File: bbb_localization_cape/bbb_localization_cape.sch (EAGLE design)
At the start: 31 parts, among them J1 CONN_04, J2 MOLEX-22-03-5035, U1 SN65HVD256DR, U2 ARDUCAMOV5642, U3 MSP430G2553IPW20R, U4 SN74LV1T126DCKR, U5 SN74LV1T125DCKR, U6 SN74LV1T126DCKR, U7 LP38693MP-3.3/NOPB, U8 LM1085ISX-ADJ

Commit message: Finished BOM
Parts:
- A1: ECE_STOCK (none) -> N; MANUFACTURER (none) -> Adafruit Industries LLC; MANUFACTURER_PART_NUMBER (none) -> 706; NOTES (none) -> 2 pack stacking header; PN (none) -> 1528-1365-ND; VENDOR (none) -> Digi-Key
- C1: ECE_STOCK (none) -> Y; LOCATION (none) -> R-3-074E, R-3-075; VENDOR (none) -> Digi-Key
- C2, C3: ECE_STOCK (none) -> N; MANUFACTURER (none) -> Murata Electronics North America; MANUFACTURER_PART_NUMBER (none) -> GRM21BR61C106KE15K; PN (none) -> 490-6473-1-ND; VENDOR (none) -> Digi-Key
- C4: ECE_STOCK (none) -> N; MANUFACTURER (none) -> Samsung Electro-Mechanics America, Inc.; MANUFACTURER_PART_NUMBER (none) -> CL21A226MOCLRNC; PN (none) -> 1276-6780-1-ND; VENDOR (none) -> Dig-Key
- C5: ECE_STOCK (none) -> Y; LOCATION (none) -> R-3-078C (D); VENDOR (none) -> Digi-Key
- C6: ECE_STOCK (none) -> N; MANUFACTURER (none) -> TDK Corporation; MANUFACTURER_PART_NUMBER (none) -> C3216X5R1A107M160AC; NOTES (none) -> Right at edge of rated voltage, consider larger form factor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; PN (none) -> 445-6007-1-ND; VENDOR (none) -> Digi-Key
- C7: ECE_STOCK (none) -> Y; LOCATION (none) -> R-3-078F; VENDOR (none) -> Digi-Key
- J1: ECE_STOCK (none) -> N; MANUFACTURER (none) -> JST Sales America Inc.; MANUFACTURER_PART_NUMBER (none) -> B4B-PH-K-S(LF)(SN); PN (none) -> 455-1706-ND; VENDOR (none) -> Digi-Key
- J2: ECE_STOCK (none) -> N; MANUFACTURER (none) -> Molex, LLC; MANUFACTURER_PART_NUMBER (none) -> 22-03-5035; PN (none) -> WM18887-ND; VENDOR (none) -> Digi-Key
- JP1: ECE_STOCK (none) -> N; MANUFACTURER (none) -> Samtec Inc.; MANUFACTURER_PART_NUMBER (none) -> SSW-104-01-F-S; PN (none) -> SAM10018-ND; VENDOR (none) -> Digi-Key
- PAD1, PAD2, SJ1, SJ2, SJ3: ECE_STOCK (none) -> N; VENDOR (none) -> OSH Park
- PS1: ECE_STOCK (none) -> N; MANUFACTURER (none) -> CUI Inc.; MANUFACTURER_PART_NUMBER (none) -> V7805-2000R; PN (none) -> 102-2188-ND; VENDOR (none) -> Digi-Key
- R1: ECE_STOCK (none) -> Y; LOCATION (none) -> R‐4‐033B; PN (none) -> P10.0KCCT‐ND; VENDOR (none) -> Digi-Key
- R2: ECE_STOCK (none) -> Y; LOCATION (none) -> R-4-033B; PN (none) -> P10.0KCCT-ND; VENDOR (none) -> Digi-Key
- R3: ECE_STOCK (none) -> Y; LOCATION (none) -> R‐4‐033B; MANUFACTURER_PART_NUMBER (none) -> ERJ-6ENF1002V; PN (none) -> P10.0KCCT-ND; VENDOR (none) -> Digi-Key
- R4: ECE_STOCK (none) -> N; MANUFACTURER (none) -> Stackpole Electronics Inc; MANUFACTURER_PART_NUMBER (none) -> RMCF0805JT47K0; NOTES (none) -> ECE stocks 0603; PN (none) -> RMCF0805JT47K0CT-ND; VENDOR (none) -> Digi-Key
- R5: ECE_STOCK (none) -> N; MANUFACTURER (none) -> Yageo; MANUFACTURER_PART_NUMBER (none) -> RC0805FR-07130RL; PN (none) -> 311-130CRCT-ND; VENDOR (none) -> Digi-Key
- R6: ECE_STOCK (none) -> N; MANUFACTURER (none) -> Yageo; MANUFACTURER_PART_NUMBER (none) -> RC0805FR-07910RL; PN (none) -> 311-910CRCT-ND; VENDOR (none) -> Digi-Key
- U1: ECE_STOCK (none) -> N; MANUFACTURER (none) -> Texas Instruments; PN (none) -> 296-30093-1-ND; VENDOR (none) -> DIGIKEY
- U2: ECE_STOCK (none) -> N; MANUFACTURER (none) -> Samtec Inc.; MANUFACTURER_PART_NUMBER (none) -> SSW-110-02-L-D; NOTES (none) -> 20 pin header; PN (none) -> SAM11952-ND; VENDOR (none) -> Digi-Key
- U3: ECE_STOCK (none) -> N; MANUFACTURER (none) -> Texas Instruments; NOTES (none) -> ECE stocks a different version; PN (none) -> 296-28430-1-ND; VENDOR (none) -> Digi-Key
- U4, U6: ECE_STOCK (none) -> N; MANUFACTURER (none) -> Texas Instruments; PN (none) -> 296-37175-1-ND; VENDOR (none) -> Digi-Key
- U5: ECE_STOCK (none) -> N; MANUFACTURER (none) -> Texas Instruments; PN (none) -> 296-37173-1-ND; VENDOR (none) -> Digi-Key
- U7: ECE_STOCK (none) -> N; MANUFACTURER (none) -> Texas Instruments; MANUFACTURER_PART_NUMBER (none) -> LP38693MP-3.3/NOPB; PN (none) -> LP38693MP-3.3/NOPBCT-ND; VENDOR (none) -> Digi-Key
- U8: ECE_STOCK (none) -> ?; MANUFACTURER (none) -> Texas Instruments; MANUFACTURER_PART_NUMBER (none) -> LM1085ISX-ADJ/NOPB; PN (none) -> LM1085ISX-ADJ/NOPBCT-ND; VENDOR (none) -> Digi-Key

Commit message: Updated pdf and other things
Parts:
- A1, C4, J2, JP1, PAD1, PAD2, PS1, R5, R6, SJ1, SJ2, SJ3, U2, U4, U5, U6: ECE_STOCK N -> (none)
- C1: ECE_STOCK Y -> (none); LOCATION R-3-074E, R-3-075 -> (none); MANUFACTURER (none) -> Samsung Electro-Mechanics America, Inc.; MANUFACTURER_PART_NUMBER (none) -> CL21B104KOANNNC; PN (none) -> 1276-2448-1-ND
- C2, C3: ECE_STOCK N -> (none); MANUFACTURER_PART_NUMBER GRM21BR61C106KE15K -> GRM21BR61E106MA73L; PN 490-6473-1-ND -> 490-10748-1-ND
- C5: ECE_STOCK Y -> (none); LOCATION R-3-078C (D) -> (none); MANUFACTURER (none) -> Samsung Electro-Mechanics America, Inc.; MANUFACTURER_PART_NUMBER (none) -> CL21B105KPFNNNE; PN (none) -> 1276-1275-1-ND
- C6: value 100uF -> 47uF; ECE_STOCK N -> (none); MANUFACTURER_PART_NUMBER C3216X5R1A107M160AC -> C3216X5R1E476M160AC; NOTES Right at edge of rated voltage, consider larger form factor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 -> Reduced capacitance from 100uF to 47uF, V2 package should b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; PN 445-6007-1-ND -> 445-8047-1-ND
- C7: ECE_STOCK Y -> (none); LOCATION R-3-078F -> (none); MANUFACTURER (none) -> Samsung Electro-Mechanics America, Inc.; MANUFACTURER_PART_NUMBER (none) -> CL21A475KQFNNNG; PN (none) -> 1276-6465-1-ND
- J1: ECE_STOCK N -> (none); MANUFACTURER_PART_NUMBER B4B-PH-K-S(LF)(SN) -> B4B-PH-K-S(LF)(SN)
- R1: ECE_STOCK Y -> (none); LOCATION R‐4‐033B -> (none); MANUFACTURER (none) -> Yageo; MANUFACTURER_PART_NUMBER (none) -> RC0805JR-0710KL; PN P10.0KCCT‐ND -> 311-10KARCT-ND
- R2: ECE_STOCK Y -> (none); LOCATION R-4-033B -> (none); MANUFACTURER (none) -> Yageo; MANUFACTURER_PART_NUMBER (none) -> RC0805JR-0710KL; PN P10.0KCCT-ND -> 311-10KARCT-ND
- R3: ECE_STOCK Y -> (none); LOCATION R‐4‐033B -> (none); MANUFACTURER (none) -> Yageo; MANUFACTURER_PART_NUMBER ERJ-6ENF1002V -> RC0805JR-0710KL; PN P10.0KCCT-ND -> 311-10KARCT-ND
- R4: ECE_STOCK N -> (none); MANUFACTURER_PART_NUMBER RMCF0805JT47K0 -> RMCF0805JT47K0; NOTES ECE stocks 0603 -> (none); PN RMCF0805JT47K0CT-ND -> RMCF0805JT47K0CT-ND
- U1: ECE_STOCK N -> (none); VENDOR DIGIKEY -> Digi-Key
- U3: ECE_STOCK N -> (none); PN 296-28430-1-ND -> 296-28430-1-ND
- U7: ECE_STOCK N -> (none); MANUFACTURER_PART_NUMBER LP38693MP-3.3/NOPB -> LP38693MP-3.3/NOPB; PN LP38693MP-3.3/NOPBCT-ND -> LP38693MP-3.3/NOPBCT-ND
- U8: ECE_STOCK ? -> (none)

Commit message: Changed board part from Adafruit to Sparkfun version
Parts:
- added B1: SPARKFUN_BEAGLE_BONE_BLACK_CAPE, SparkFun-Boards:SPARKFUN_BEAGLE_BONE_BLACK_CAPE
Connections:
- net +5V: now also B1P9.VDD_5V@1, B1P9.VDD_5V@2
- net DCAN1_RX: now also B1P9.GPIO_15
- net DCAN1_TX: now also B1P9.GPIO_14
- net GND: now also B1P8.DGND@1, B1P8.DGND@2, B1P9.DGND@1, B1P9.DGND@2, B1P9.DGND@3, B1P9.DGND@4, B1P9.DGND@5, B1P9.DGND@6
- net I2C2_SCL: now also B1P9.I2C2_SCL
- net I2C2_SDA: now also B1P9.I2C2_SDA
- net PRU1_0: now also B1P8.GPIO_70
- net PRU1_1: now also B1P8.GPIO_71
- net PRU1_10: now also B1P8.GPIO_88
- net PRU1_2: now also B1P8.GPIO_72
- net PRU1_3: now also B1P8.GPIO_73
- net PRU1_4: now also B1P8.GPIO_74
- net PRU1_5: now also B1P8.GPIO_75
- net PRU1_6: now also B1P8.GPIO_76
- net PRU1_7: now also B1P8.GPIO_77
- net PRU1_8: now also B1P8.GPIO_86
- net PRU1_9: now also B1P8.GPIO_87
- net PWDN: now also B1P8.GPIO_32
- net SYS_RESETN: now also B1P9.SYS_RESET!N
- net TIMER4: now also B1P8.GPIO_66
- net UART2_DIR: now also B1P9.GPIO_49
- net UART2_RXD: now also B1P9.GPIO_2
- net UART2_TXD: now also B1P9.GPIO_3

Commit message: Finished changing cape style
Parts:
- removed A1: BEAGLEBONE_OUTLINE, bbb_localization_cape:BEAGLEBONE_OUTLINE
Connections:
- net +5V: no longer A1.05.VDD_5V@P9, A1.VDD_5V.06@P9
- net DCAN1_RX: no longer A1.24@P9
- net DCAN1_TX: no longer A1.26@P9
- net GND: no longer A1.01.DGND@P8, A1.01.DGND@P9, A1.43.DGND@P9, A1.45.DGND@P9, A1.DGND.02@P8, A1.DGND.44@P9, A1.DGND.46@P9, A1.GND.02@P9
- net I2C2_SCL: no longer A1.19@P9
- net I2C2_SDA: no longer A1.20@P9
- net PRU1_0: no longer A1.45@P8
- net PRU1_1: no longer A1.46@P8
- net PRU1_10: no longer A1.28@P8
- net PRU1_2: no longer A1.43@P8
- net PRU1_3: no longer A1.44@P8
- net PRU1_4: no longer A1.41@P8
- net PRU1_5: no longer A1.42@P8
- net PRU1_6: no longer A1.39@P8
- net PRU1_7: no longer A1.40@P8
- net PRU1_8: no longer A1.27@P8
- net PRU1_9: no longer A1.29@P8
- net PWDN: no longer A1.25@P8
- net SYS_RESETN: no longer A1.SYS_RESETN.10@P9
- net TIMER4: no longer A1.07@P8
- net UART2_DIR: no longer A1.23@P9
- net UART2_RXD: no longer A1.22@P9
- net UART2_TXD: no longer A1.21@P9
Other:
- moved on the sheet: B1P8, B1P9

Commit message: Added reverse current protection and changed PWDN pin
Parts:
- added D1: (no value), diode:DIODE-DO-214AC
- C6: value 47uF -> 100uF; device rcl:C-USC1206 -> resistor:CPOL-USE
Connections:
- new net N$4: D1.A, PAD1.P
- net +10V: now also C6.+; no longer C6.1
- net +12V: now also D1.C; no longer PAD1.P
- net GND: now also C6.-; no longer C6.2
- net PWDN: now also B1P8.GPIO_61; no longer B1P8.GPIO_32

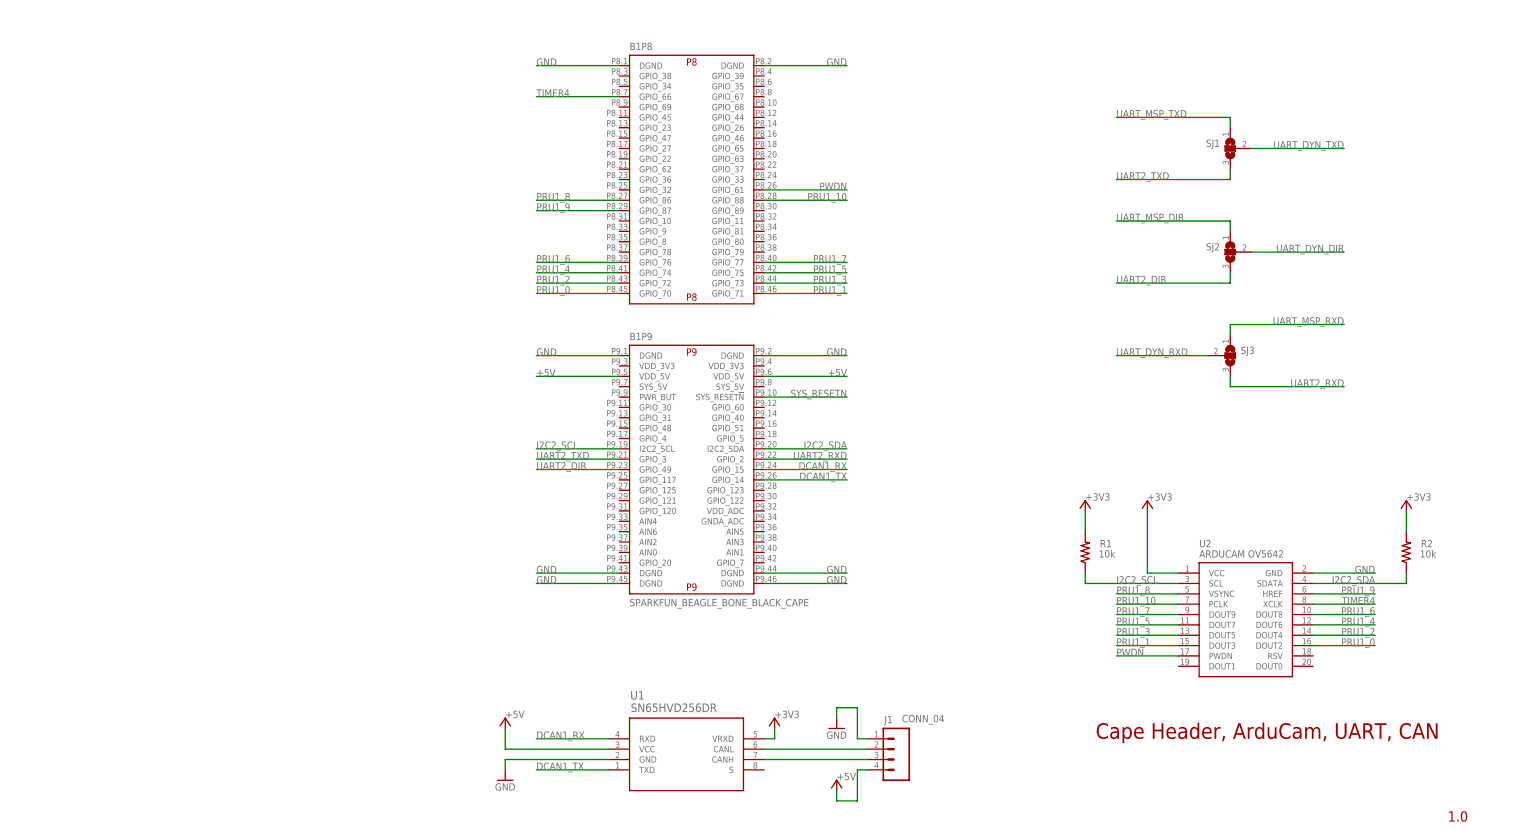
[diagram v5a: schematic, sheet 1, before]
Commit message: Changed XCLK
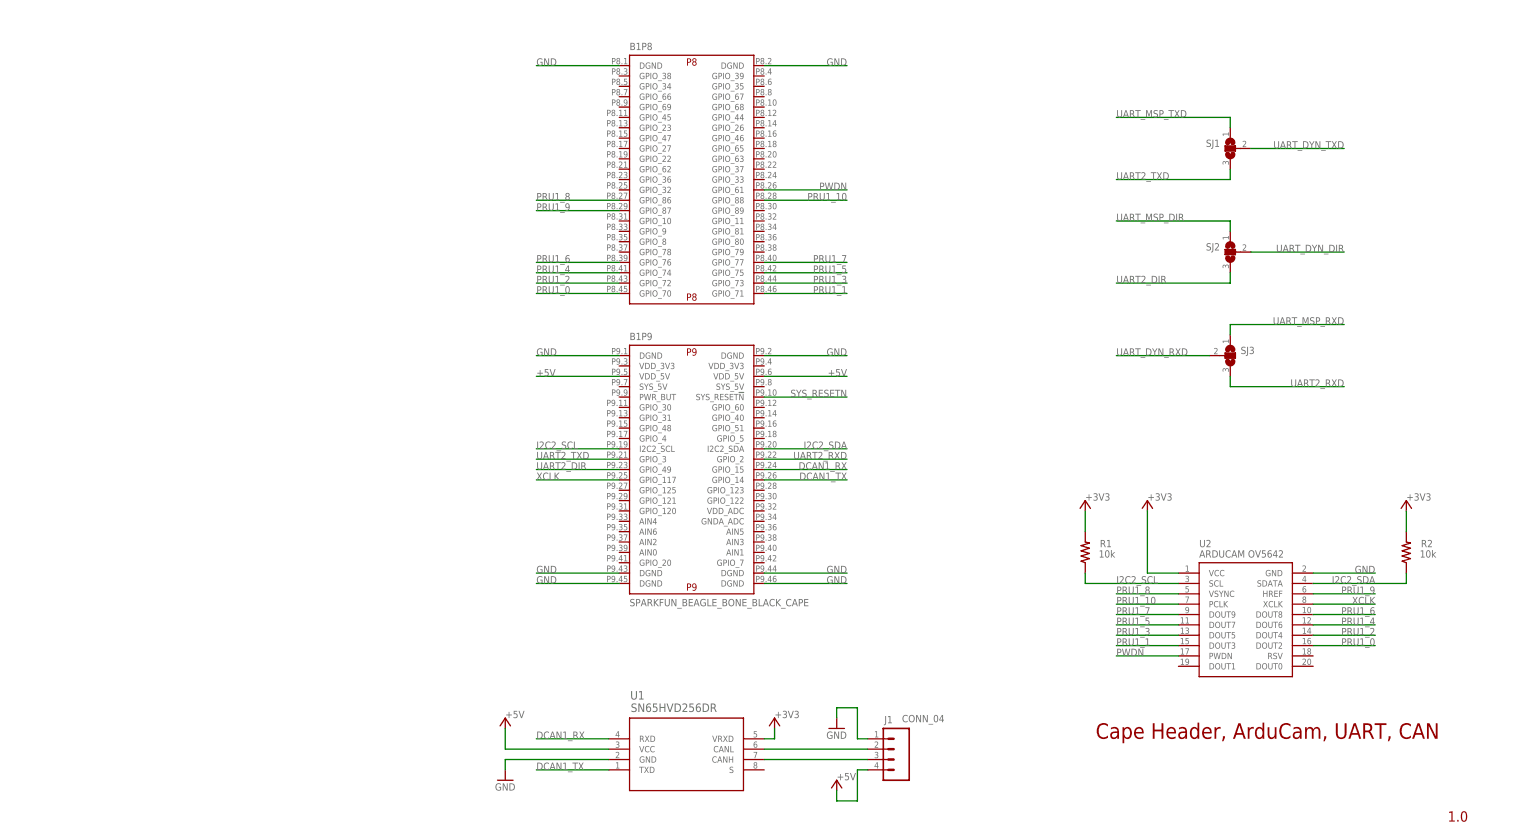
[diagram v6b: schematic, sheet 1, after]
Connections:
- removed net TIMER4: B1P8.GPIO_66, U2.XCLK
- new net XCLK: B1P9.GPIO_117, U2.XCLK
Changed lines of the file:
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@@
-</segment>
-</net>
-<net name="TIMER4" class="1">
-<segment>
-<pinref part="U2" gate="&gt;NAME" pin="XCLK"/>
-<wire x1="231.14" y1="60.96" x2="246.38" y2="60.96" width="0.1524" layer="91"/>
-<label x="246.38" y="60.96" size="1.778" layer="95" rot="MR0"/>
-</segment>
-<segment>
-<pinref part="B1" gate="P8" pin="GPIO_66"/>
-<wire x1="60.96" y1="185.42" x2="40.64" y2="185.42" width="0.1524" layer="91"/>
-<label x="40.64" y="185.42" size="1.778" layer="95"/>
 </segment>
 </net>
@@
 </segment>
 </net>
+<net name="XCLK" class="0">
+<segment>
+<pinref part="B1" gate="P9" pin="GPIO_117"/>
+<wire x1="60.96" y1="91.44" x2="40.64" y2="91.44" width="0.1524" layer="91"/>
+<label x="40.64" y="91.44" size="1.778" layer="95"/>
+</segment>
+<segment>
+<pinref part="U2" gate="&gt;NAME" pin="XCLK"/>
+<wire x1="231.14" y1="60.96" x2="246.38" y2="60.96" width="0.1524" layer="91"/>
+<label x="246.38" y="60.96" size="1.778" layer="95" rot="MR0"/>
+</segment>
+</net>

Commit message: Added dimension layer
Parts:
- C6: SPICEPREFIX (none) -> C
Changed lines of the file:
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@@
 <setting verticaltext="up"/>
 </settings>
-<grid distance="0.1" unitdist="inch" unit="inch" style="dots" multiple="1" display="yes" altdistance="0.01" altunitdist="inch" altunit="inch"/>
+<grid distance="0.1" unitdist="inch" unit="inch" style="lines" multiple="1" display="no" altdistance="0.01" altunitdist="inch" altunit="inch"/>
 <layers>
 <layer number="1" name="Top" color="4" fill="1" visible="yes" active="no"/>
@@
 <attribute name="NOTES" value="Reduced capacitance from 100uF to 47uF, V2 package should be 1210 or larger"/>
 <attribute name="PN" value="445-8047-1-ND"/>
-<attribute name="VENDOR" value="Digi-Key"/>
-</part>
+<attribute name="SPICEPREFIX" value="C"/>
+<attribute name="VENDOR" value="Digi-Key"/>
+</part>

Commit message: Updated 3D models
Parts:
- B1: device SparkFun-Boards:SPARKFUN_BEAGLE_BONE_BLACK_CAPE -> bbb_localization_cape:SPARKFUN_BEAGLE_BONE_BLACK_CAPE
- C6: device resistor:CPOL-USE -> bbb_localization_cape:CAP_PANASONIC_E
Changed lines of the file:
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@@
 <attribute name="VENDOR" value="Dig-Key"/>
 </part>
-<part name="C6" library="resistor" library_urn="urn:adsk.eagle:library:348" deviceset="CPOL-US" device="E" package3d_urn="urn:adsk.eagle:package:25915/1" value="100uF">
+<part name="C6" library="bbb_localization_cape" library_urn="urn:adsk.eagle:library:616562" deviceset="CAP" device="PANASONIC_E" package3d_urn="urn:adsk.eagle:package:988760/2" technology="_" value="100uF">
 <attribute name="MANUFACTURER" value="TDK Corporation"/>
 <attribute name="MANUFACTURER_PART_NUMBER" value="C3216X5R1E476M160AC"/>
@@
 <part name="GND10" library="supply1" library_urn="urn:adsk.eagle:library:371" deviceset="GND" device=""/>
 <part name="P+7" library="supply1" library_urn="urn:adsk.eagle:library:371" deviceset="+5V" device=""/>
-<part name="B1" library="SparkFun-Boards" library_urn="urn:adsk.eagle:library:509" deviceset="SPARKFUN_BEAGLE_BONE_BLACK_CAPE" device="" package3d_urn="urn:adsk.eagle:package:37329/1"/>
+<part name="B1" library="bbb_localization_cape" library_urn="urn:adsk.eagle:library:616562" deviceset="SPARKFUN_BEAGLE_BONE_BLACK_CAPE" device="" package3d_urn="urn:adsk.eagle:package:988767/2"/>
 <part name="D1" library="diode" library_urn="urn:adsk.eagle:library:210" deviceset="DIODE-" device="DO-214AC" package3d_urn="urn:adsk.eagle:package:43416/2"/>
 </parts>
